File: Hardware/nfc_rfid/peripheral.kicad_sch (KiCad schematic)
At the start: 37 parts, among them IC2 FAN48610BUC50X, J3 HC-FPC-05-09-18RLTAG, J4 Vibro_+, J5 Vibro_-, Q1 AO3400A

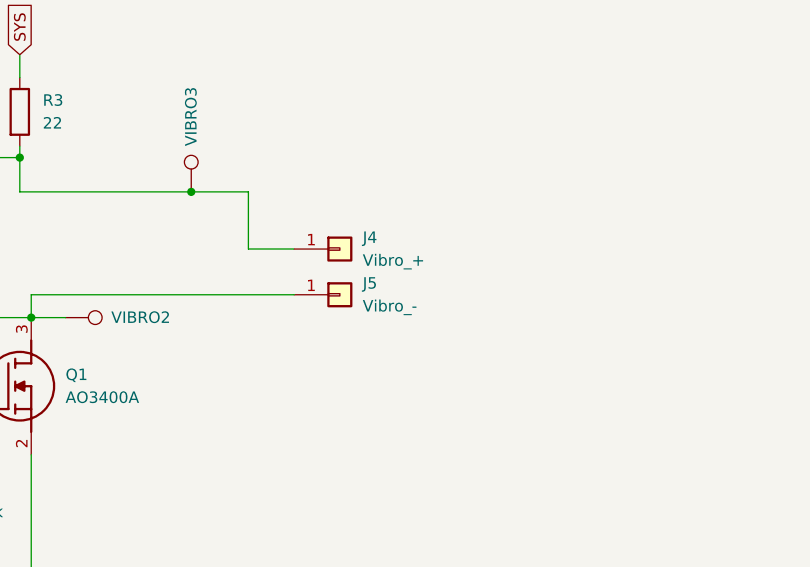
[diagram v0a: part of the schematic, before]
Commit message: PCB: Components placing done
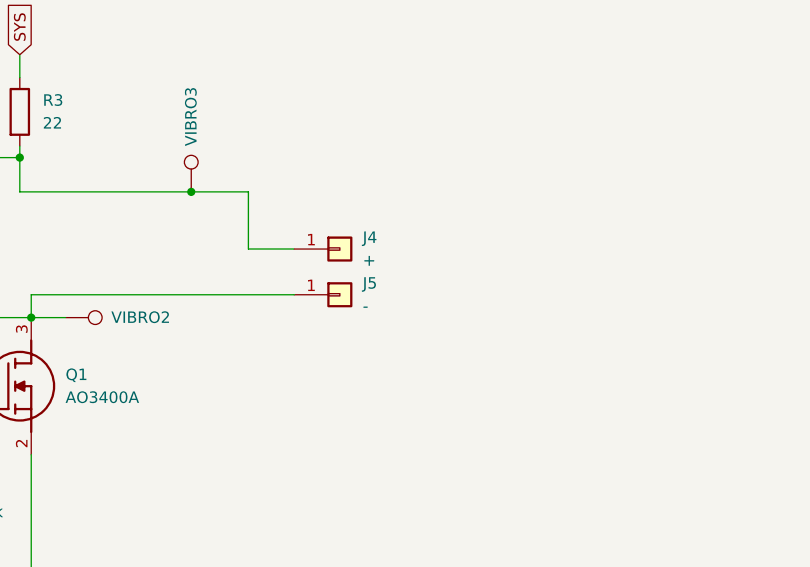
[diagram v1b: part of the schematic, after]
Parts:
- J3: footprint SamacSys_Parts:FH34SRJ18S05SH50 -> Library:CONN18x1_FH34SRJ-18S-0.5SH50_HIR
- J4: value Vibro_+ -> +; footprint Library:SMD_L3.4-W0.9 -> Library:TestPoint_Pad_3.0x2.0mm_round_corner_no_silkscreen; now left out of the parts list
- J5: value Vibro_- -> -; footprint Library:SMD_L3.4-W0.9 -> Library:TestPoint_Pad_3.0x2.0mm_round_corner_no_silkscreen; now left out of the parts list
- L3: footprint Inductor_SMD:L_0402_1005Metric -> Inductor_SMD:L_Murata_DFE201610P
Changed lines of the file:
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@@
 			)
 		)
-		(property "Footprint" "SamacSys_Parts:FH34SRJ18S05SH50"
+		(property "Footprint" "Library:CONN18x1_FH34SRJ-18S-0.5SH50_HIR"
 			(at 59.69 -12.37 0)
 			(effects
@@
 			)
 		)
-		(property "Footprint" "Inductor_SMD:L_0402_1005Metric"
+		(property "Footprint" "Inductor_SMD:L_Murata_DFE201610P"
 			(at 44.45 146.05 0)
 			(effects
@@
 		(unit 1)
 		(exclude_from_sim no)
-		(in_bom yes)
+		(in_bom no)
 		(on_board yes)
 		(dnp no)
@@
 			)
 		)
-		(property "Value" "Vibro_-"
+		(property "Value" "-"
 			(at 223.52 50.7999 0)
 			(effects
@@
 			)
 		)
-		(property "Footprint" "Library:SMD_L3.4-W0.9"
+		(property "Footprint" "Library:TestPoint_Pad_3.0x2.0mm_round_corner_no_silkscreen"
 			(at 220.98 49.53 0)
 			(effects
@@
 		(unit 1)
 		(exclude_from_sim no)
-		(in_bom yes)
+		(in_bom no)
 		(on_board yes)
 		(dnp no)
@@
 			)
 		)
-		(property "Value" "Vibro_+"
+		(property "Value" "+"
 			(at 223.52 45.7199 0)
 			(effects
@@
 			)
 		)
-		(property "Footprint" "Library:SMD_L3.4-W0.9"
+		(property "Footprint" "Library:TestPoint_Pad_3.0x2.0mm_round_corner_no_silkscreen"
 			(at 220.98 44.45 0)
 			(effects

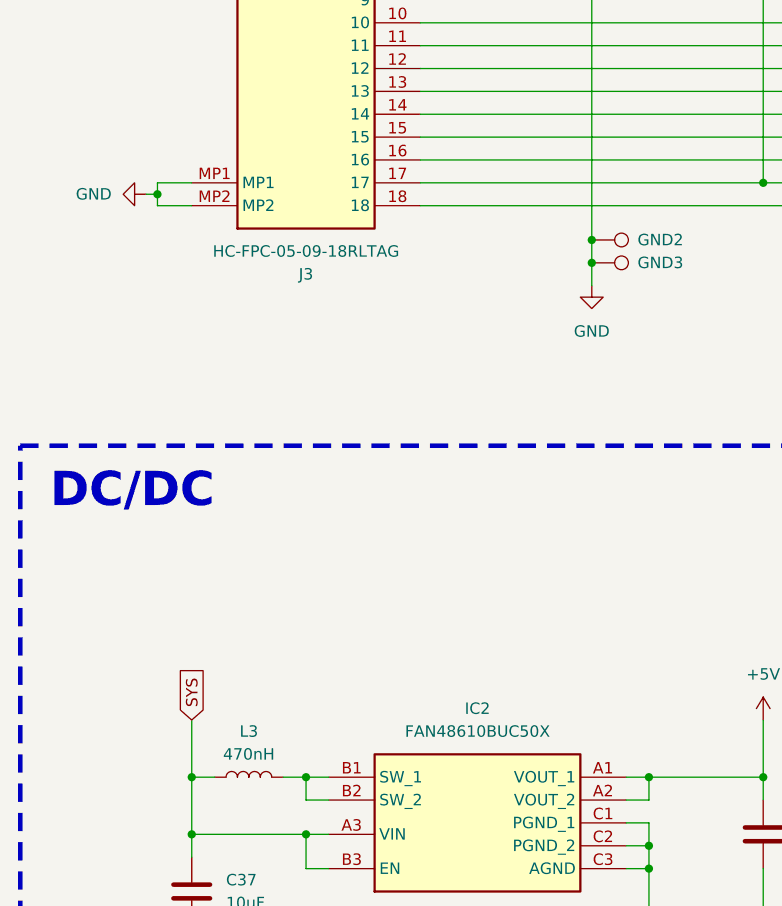
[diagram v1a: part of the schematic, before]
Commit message: PCB: add "remove from bom" entity; adjust design rule
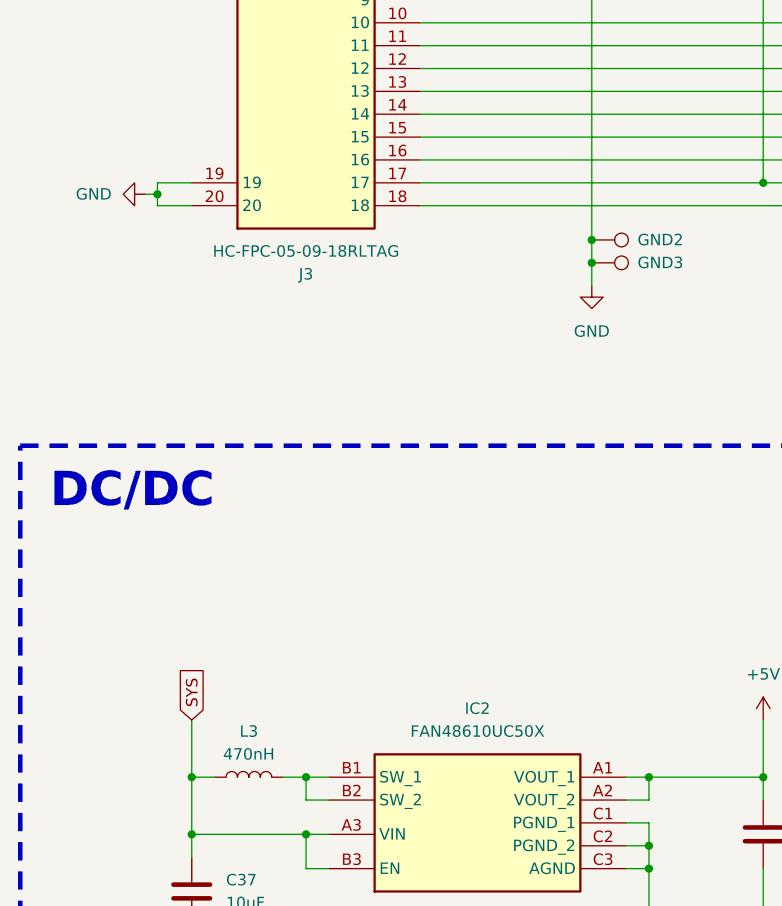
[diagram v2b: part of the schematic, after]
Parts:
- IC2: value FAN48610BUC50X -> FAN48610UC50X
- TP10, TP11, TP12, TP13, TP14, TP15, TP16, TP17, TP18, TP19, TP20, TP21, TP22, TP23, TP24, TP25, TP26, TP27, TP28, TP29, TP30, TP6, TP7, TP8, TP9: now left out of the parts list
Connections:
- net GND: now also J3.19, J3.20; no longer J3.MP1, J3.MP2
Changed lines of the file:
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@@
 		(unit 1)
 		(exclude_from_sim no)
-		(in_bom yes)
+		(in_bom no)
 		(on_board yes)
 		(dnp no)
@@
 		(unit 1)
 		(exclude_from_sim no)
-		(in_bom yes)
+		(in_bom no)
 		(on_board yes)
 		(dnp no)
@@
 		(unit 1)
 		(exclude_from_sim no)
-		(in_bom yes)
+		(in_bom no)
 		(on_board yes)
 		(dnp no)
@@
 		(unit 1)
 		(exclude_from_sim no)
-		(in_bom yes)
+		(in_bom no)
 		(on_board yes)
 		(dnp no)
@@
 		(pin "12"
 		)
-		(pin "MP1"
+		(pin "20"
 		)
 		(pin "16"
@@
 		(pin "5"
 		)
-		(pin "MP2"
+		(pin "19"
 		)
 		(pin "18"
@@
 		(unit 1)
 		(exclude_from_sim no)
-		(in_bom yes)
+		(in_bom no)
 		(on_board yes)
 		(dnp no)
@@
 		(unit 1)
 		(exclude_from_sim no)
-		(in_bom yes)
+		(in_bom no)
 		(on_board yes)
 		(dnp no)
@@
 		(unit 1)
 		(exclude_from_sim no)
-		(in_bom yes)
+		(in_bom no)
 		(on_board yes)
 		(dnp no)
@@
 		(unit 1)
 		(exclude_from_sim no)
-		(in_bom yes)
+		(in_bom no)
 		(on_board yes)
 		(dnp no)
@@
 		(unit 1)
 		(exclude_from_sim no)
-		(in_bom yes)
+		(in_bom no)
 		(on_board yes)
 		(dnp no)
@@
 		(unit 1)
 		(exclude_from_sim no)
-		(in_bom yes)
+		(in_bom no)
 		(on_board yes)
 		(dnp no)
@@
 		(unit 1)
 		(exclude_from_sim no)
-		(in_bom yes)
+		(in_bom no)
 		(on_board yes)
 		(dnp no)
@@
 		(unit 1)
 		(exclude_from_sim no)
-		(in_bom yes)
+		(in_bom no)
 		(on_board yes)
 		(dnp no)
@@
 		(unit 1)
 		(exclude_from_sim no)
-		(in_bom yes)
+		(in_bom no)
 		(on_board yes)
 		(dnp no)
@@
 		(unit 1)
 		(exclude_from_sim no)
-		(in_bom yes)
+		(in_bom no)
 		(on_board yes)
 		(dnp no)
@@
 		(unit 1)
 		(exclude_from_sim no)
-		(in_bom yes)
+		(in_bom no)
 		(on_board yes)
 		(dnp no)
@@
 			)
 		)
-		(property "Value" "FAN48610BUC50X"
+		(property "Value" "FAN48610UC50X"
 			(at 69.85 140.97 0)
 			(effects
@@
 		(unit 1)
 		(exclude_from_sim no)
-		(in_bom yes)
+		(in_bom no)
 		(on_board yes)
 		(dnp no)
@@
 		(unit 1)
 		(exclude_from_sim no)
-		(in_bom yes)
+		(in_bom no)
 		(on_board yes)
 		(dnp no)
@@
 		(unit 1)
 		(exclude_from_sim no)
-		(in_bom yes)
+		(in_bom no)
 		(on_board yes)
 		(dnp no)
@@
 		(unit 1)
 		(exclude_from_sim no)
-		(in_bom yes)
+		(in_bom no)
 		(on_board yes)
 		(dnp no)
@@
 		(unit 1)
 		(exclude_from_sim no)
-		(in_bom yes)
+		(in_bom no)
 		(on_board yes)
 		(dnp no)
@@
 		(unit 1)
 		(exclude_from_sim no)
-		(in_bom yes)
+		(in_bom no)
 		(on_board yes)
 		(dnp no)
@@
 		(unit 1)
 		(exclude_from_sim no)
-		(in_bom yes)
+		(in_bom no)
 		(on_board yes)
 		(dnp no)
@@
 		(unit 1)
 		(exclude_from_sim no)
-		(in_bom yes)
+		(in_bom no)
 		(on_board yes)
 		(dnp no)
@@
 		(unit 1)
 		(exclude_from_sim no)
-		(in_bom yes)
+		(in_bom no)
 		(on_board yes)
 		(dnp no)
@@
 		(unit 1)
 		(exclude_from_sim no)
-		(in_bom yes)
+		(in_bom no)
 		(on_board yes)
 		(dnp no)
